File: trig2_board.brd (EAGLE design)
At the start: 80 x 96 mm, 32 parts, among them IC1 SN74ACT244DW, J1 2p-2.54, J10 2p-2.54, J11 2p-2.54, J12 2p-2.54, J13 8pin, J2 2p-2.54, J3 2p-2.54, J4 2p-2.54, J5 2p-2.54, J6 2p-2.54, J7 2p-2.54, J8 2p-2.54, J9 2p-2.54, X1 BU-SMB-V, X10 BU-SMB-V, X11 BU-SMB-V, X12 BU-SMB-V, X13 87758-2816, X14 87758-2816, X15 87758-1616, X16 87758-1616, X17 87758-2816, X18 87758-2816, X2 BU-SMB-V, X3 BU-SMB-V, X4 BU-SMB-V, X5 BU-SMB-V, X6 BU-SMB-V, X7 BU-SMB-V, X8 BU-SMB-V, X9 BU-SMB-V

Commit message: autorouted with topo
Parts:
- removed IC1: SN74ACT244DW, SN74ACT244DW:SOIC127P1030X265-20N
- removed J10, J11, J12, J9: 2p-2.54, Seeed-Connector:H2-2.54
- removed X10, X11, X12, X9: BU-SMB-V, con-coax:BU-SMB-V
- added 106OUT1, 176OUT2, 181OUT3, 183OUT4: BU-SMB-V, con-coax:BU-SMB-V
- added C1: (no value), SparkFun-Capacitors:0805
- added OJ1, OJ2, OJ3, OJ4: 2p-2.54, Seeed-Connector:H2-2.54
- added VSLUE: SN74ACT244DW, SN74ACT244DW:SOIC127P1030X265-20N
- moved J8 40.2 mm to (65.1, 91.0)
- moved X8 40.2 mm to (64.1, 86.0)
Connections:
- removed net IO106: J11.1, X11.1, X14.23
- removed net IO176: J10.1, X10.1, X13.7
- removed net IO181: J9.1, X13.5, X9.1
- removed net IO183: J8.1, X13.3, X8.1
- removed net VCC: IC1.20
- new net IO106_IN1: VSLUE.2, VSLUE.4, X14.23
- new net IO176_IN2: VSLUE.6, VSLUE.8, X13.7
- new net IO181_IN3: VSLUE.11, VSLUE.13, X13.5
- new net IO183_IN4: VSLUE.15, VSLUE.17, X13.3
- new net OUT1: 106OUT1.1, OJ1.1, VSLUE.16, VSLUE.18
- new net OUT2: 176OUT2.1, OJ2.1, VSLUE.12, VSLUE.14
- new net OUT3: 181OUT3.1, OJ3.1, VSLUE.7, VSLUE.9
- new net OUT4: 183OUT4.1, OJ4.1, VSLUE.3, VSLUE.5
- net 5V: now also C1.2, VSLUE.20
- net GND: now also 106OUT1.2, 106OUT1.3, 106OUT1.4, 106OUT1.5, 176OUT2.2, 176OUT2.3, 176OUT2.4, 176OUT2.5, 181OUT3.2, 181OUT3.3, 181OUT3.4, 181OUT3.5, 183OUT4.2, 183OUT4.3, 183OUT4.4, 183OUT4.5, C1.1, OJ1.2, OJ2.2, OJ3.2, OJ4.2, VSLUE.1, VSLUE.10, VSLUE.19; no longer IC1.10, J10.2, J11.2, J12.2, J9.2, X10.2, X10.3, X10.4, X10.5, X11.2, X11.3, X11.4, X11.5, X12.2, X12.3, X12.4, X12.5, X9.2, X9.3, X9.4, X9.5
- net IO102: now also J8.1, X8.1; no longer J12.1, X12.1
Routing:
- net IO106_IN1: track 0.00 -> 82.2 mm
- net IO181_IN3: track 0.00 -> 44.8 mm
- net IO183_IN4: track 0.00 -> 39.7 mm
- net 3V3: track 100.3 -> 64.7 mm, vias 0 -> 2
- net IO106: track 33.4 -> 0.00 mm
- net IO176: track 32.0 -> 0.00 mm
- net 5V: track 128.2 -> 159.8 mm
- net IO176_IN2: track 0.00 -> 30.9 mm
- net IO181: track 23.4 -> 0.00 mm
- net GND: track 0.00 -> 22.1 mm
- net IO183: track 21.0 -> 0.00 mm
- net OUT1: track 0.00 -> 19.2 mm
- net OUT4: track 0.00 -> 17.4 mm
- net OUT2: track 0.00 -> 16.8 mm
- net OUT3: track 0.00 -> 16.7 mm
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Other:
- board size 80 x 96 mm -> 80 x 123 mm
- board text removed: "106"
- board text removed: "176"
- board text removed: "181"
- board text removed: "183"

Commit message: with design block
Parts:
- removed 106OUT1, 176OUT2, 181OUT3, 183OUT4, X7, X8: BU-SMB-V, con-coax:BU-SMB-V
- removed J7, J8: 2p-2.54, Seeed-Connector:H2-2.54
- added 174OUT, 175OUT, 176OUT, 177OUT, 181OUT, 182OUT, 183OUT, 184OUT: BU-SMB-V, con-coax:BU-SMB-V
- added C3: 0.1uF, SparkFun-Capacitors:0805
- added OJ10, OJ11, OJ12, OJ9: 2p-2.54, Seeed-Connector:H2-2.54
- added VSLUE2: SN74ACT244DW, SN74ACT244DW:SOIC127P1030X265-20N
- C1: value (none) -> 0.1uF
- moved OJ1 105.6 mm to (120.0, 72.9), turned to 0 degrees
- moved OJ2 101.8 mm to (120.0, 63.0), turned to 0 degrees
- moved C1 91.4 mm to (107.0, 78.0), turned to 270 degrees
- moved VSLUE 79.7 mm to (102.0, 69.0), turned to 0 degrees
- moved J6 67.3 mm to (5.79, 7.95), turned to 0 degrees
- moved X6 63.5 mm to (10.7, 6.91), turned to 90 degrees
- moved OJ4 60.0 mm to (84.0, 73.1), turned to 0 degrees
- moved J5 58.7 mm to (5.79, 18.0), turned to 0 degrees
- moved J13 56.5 mm to (56.0, 77.0), turned to 0 degrees
- moved J1 56.1 mm to (5.79, 58.2), turned to 0 degrees
- moved X14 54.9 mm to (73.0, 18.0), turned to 270 degrees
- moved X5 53.9 mm to (10.7, 17.0), turned to 90 degrees
- moved OJ3 53.0 mm to (84.0, 63.0), turned to 0 degrees
- moved J4 52.6 mm to (5.79, 28.1), turned to 0 degrees
- moved J2 51.1 mm to (5.79, 48.2), turned to 0 degrees
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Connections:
- removed net IO100: J7.1, X14.27, X7.1
- removed net IO102: J8.1, X14.25, X8.1
- removed net IO106_IN1: VSLUE.2, VSLUE.4, X14.23
- new net IO174_IN1: VSLUE.2, VSLUE.4, X13.9
- new net IO175_IN1: VSLUE2.2, VSLUE2.4, X13.10
- new net IO177_IN2: VSLUE2.6, VSLUE2.8, X13.8
- new net IO182_IN3: VSLUE2.11, VSLUE2.13, X13.6
- new net IO184_IN4: VSLUE2.15, VSLUE2.17, X13.4
- new net OUT5: 175OUT.1, OJ12.1, VSLUE2.16, VSLUE2.18
- new net OUT6: 177OUT.1, OJ11.1, VSLUE2.12, VSLUE2.14
- new net OUT7: 182OUT.1, OJ10.1, VSLUE2.7, VSLUE2.9
- new net OUT8: 184OUT.1, OJ9.1, VSLUE2.3, VSLUE2.5
- net 3V3: no longer X18.2
- net 5V: now also C3.2, J13.7, VSLUE2.20; no longer J13.1
- net GND: now also 174OUT.2, 174OUT.3, 174OUT.4, 174OUT.5, 175OUT.2, 175OUT.3, 175OUT.4, 175OUT.5, 176OUT.2, 176OUT.3, 176OUT.4, 176OUT.5, 177OUT.2, 177OUT.3, 177OUT.4, 177OUT.5, 181OUT.2, 181OUT.3, 181OUT.4, 181OUT.5, 182OUT.2, 182OUT.3, 182OUT.4, 182OUT.5, 183OUT.2, 183OUT.3, 183OUT.4, 183OUT.5, 184OUT.2, 184OUT.3, 184OUT.4, 184OUT.5, C3.1, J13.5, J13.6, OJ10.2, OJ11.2, OJ12.2, OJ9.2, VSLUE2.1, VSLUE2.10, VSLUE2.19; no longer 106OUT1.2, 106OUT1.3, 106OUT1.4, 106OUT1.5, 176OUT2.2, 176OUT2.3, 176OUT2.4, 176OUT2.5, 181OUT3.2, 181OUT3.3, 181OUT3.4, 181OUT3.5, 183OUT4.2, 183OUT4.3, 183OUT4.4, 183OUT4.5, J13.2, J13.7, J7.2, J8.2, X7.2, X7.3, X7.4, X7.5, X8.2, X8.3, X8.4, X8.5
- net IO186: now also J13.1; no longer J13.3
- net IO188: now also J13.2; no longer J13.4
- net IO194: now also J13.3; no longer J13.5
- net IO196: now also J13.4; no longer J13.6
- net OUT1: now also 174OUT.1; no longer 106OUT1.1
- net OUT2: now also 176OUT.1; no longer 176OUT2.1
- net OUT3: now also 181OUT.1; no longer 181OUT3.1
- net OUT4: now also 183OUT.1; no longer 183OUT4.1
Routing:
- net IO106_IN1: track 82.2 -> 0.00 mm
- net IO182_IN3: track 0.00 -> 57.5 mm
- net IO174_IN1: track 0.00 -> 47.1 mm
- net 3V3: track 64.7 -> 21.2 mm, vias 2 -> 0
- net IO184_IN4: track 0.00 -> 41.2 mm, vias 0 -> 1
- net IO175_IN1: track 0.00 -> 39.2 mm
- net IO177_IN2: track 0.00 -> 32.4 mm
- net GND: track 22.1 -> 49.0 mm
- net IO102: track 24.3 -> 0.00 mm
- net OUT8: track 0.00 -> 23.8 mm
- net OUT5: track 0.00 -> 23.8 mm
- net OUT6: track 0.00 -> 23.3 mm
- net OUT7: track 0.00 -> 23.2 mm
- net IO100: track 21.1 -> 0.00 mm
- net IO183_IN4: track 39.7 -> 57.6 mm, vias 0 -> 1
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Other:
- board size 80 x 123 mm -> 123 x 80 mm
- board text removed: "100"
- board text removed: "102"

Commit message: better routing
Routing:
- net IO183_IN4: track 57.6 -> 42.7 mm
- net OUT4: track 28.8 -> 18.7 mm
- net IO182_IN3: track 57.5 -> 48.4 mm, vias 0 -> 1
- net OUT7: track 23.2 -> 18.0 mm
- net OUT8: track 23.8 -> 18.7 mm
- net IO176_IN2: track 41.6 -> 36.5 mm
- net GND: track 49.0 -> 53.3 mm
- net IO175_IN1: track 39.2 -> 35.0 mm
- net IO181_IN3: track 45.9 -> 41.7 mm
- net OUT6: track 23.3 -> 19.2 mm
- net OUT5: track 23.8 -> 20.0 mm
- net IO177_IN2: track 32.4 -> 29.3 mm
- net IO194: track 24.5 -> 21.5 mm
- net 3V3: track 21.2 -> 18.8 mm
- net OUT1: track 19.1 -> 21.5 mm, vias 0 -> 1
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
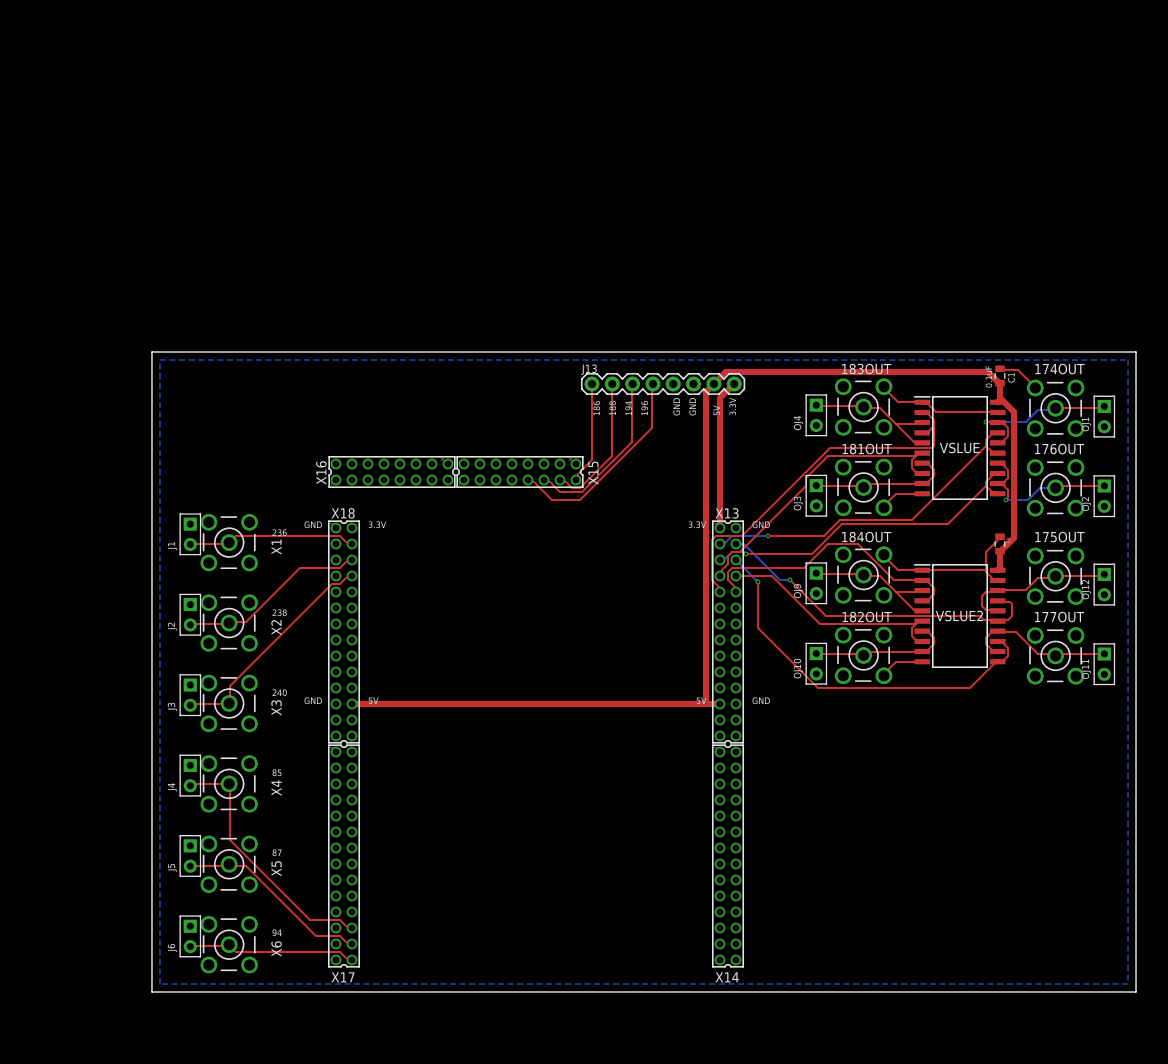
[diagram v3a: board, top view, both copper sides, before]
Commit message: 16 inputs and 16 outputs
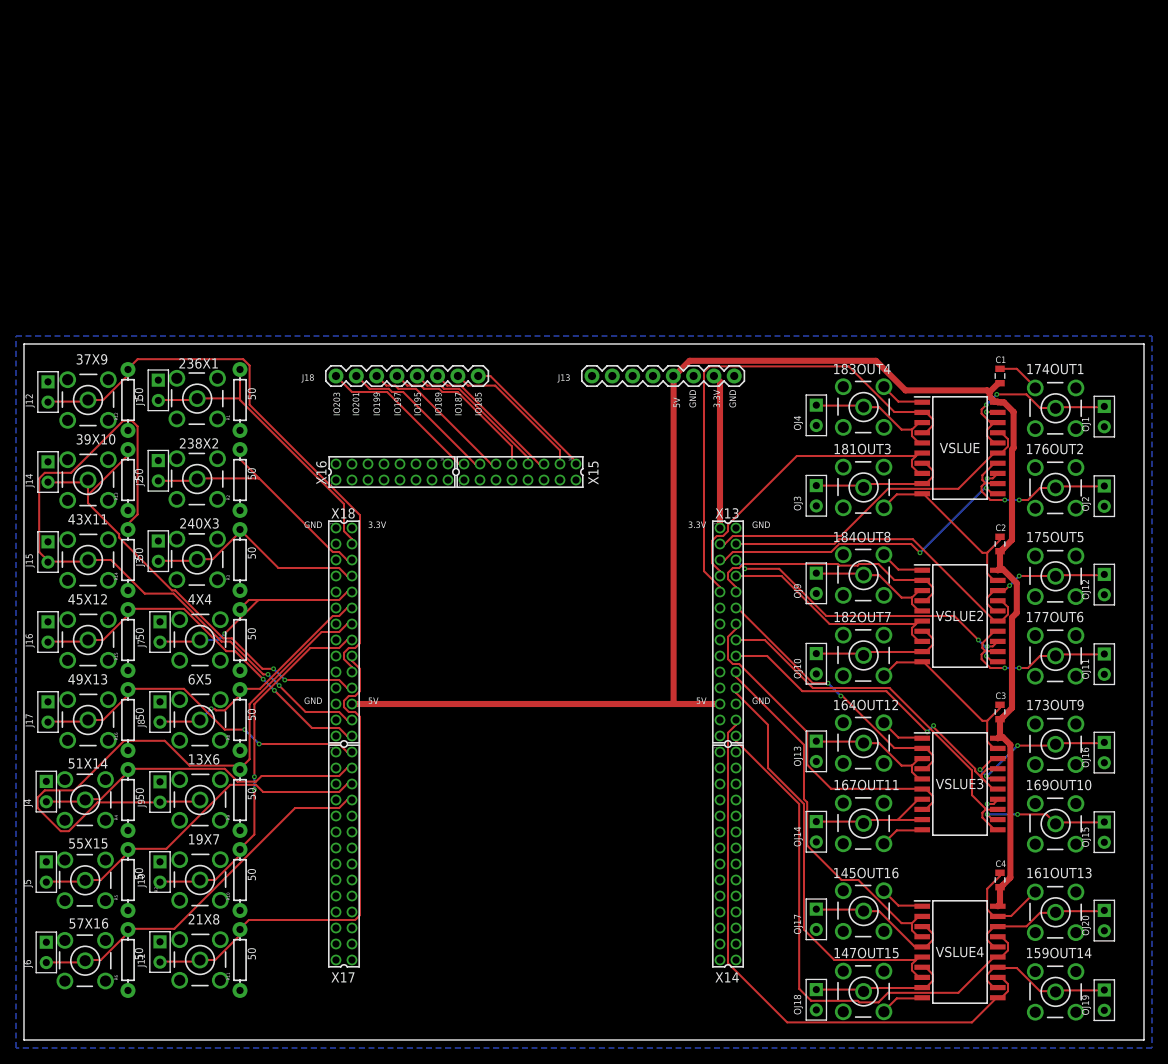
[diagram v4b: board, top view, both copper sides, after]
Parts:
- removed X1, X2, X3, X4, X5, X6: BU-SMB-V, con-coax:BU-SMB-V
- added 13X6, 145OUT16, 147OUT15, 159OUT14, 161OUT13, 164OUT12, 167OUT11, 169OUT10, 173OUT9, 19X7, 21X8, 236X1, 238X2, 240X3, 37X9, 39X10, 43X11, 45X12, 49X13, 4X4, 51X14, 55X15, 57X16, 6X5: BU-SMB-V, con-coax:BU-SMB-V
- added C2, C4: 0.1uF, SparkFun-Capacitors:0805
- added J10, J11, J12, J14, J15, J16, J17, J7, J8, J9, OJ13, OJ14, OJ15, OJ16, OJ17, OJ18, OJ19, OJ20: 2p-2.54, Seeed-Connector:H2-2.54
- added J18: 8pin, SparkFun-Connectors:1X08
- added R1, R10, R11, R12, R13, R14, R15, R16, R2, R3, R4, R5, R6, R7, R8, R9: 50, SparkFun-Passives:AXIAL-0.3
- added VSLUE3, VSLUE4: SN74ACT244DW, SN74ACT244DW:SOIC127P1030X265-20N
- moved C3 21.0 mm to (107.0, 36.0)
- moved J2 18.4 mm to (1.79, 66.2)
- moved J3 18.4 mm to (1.79, 56.1)
- moved J1 18.4 mm to (1.79, 76.2)
- moved J4 18.1 mm to (-12.2, 26.1)
- moved J5 18.1 mm to (-12.2, 16.0)
- moved J6 18.1 mm to (-12.2, 5.95)
- moved J13 1.00 mm to (56.0, 78.0)
- renumbered 174OUT to 174OUT1, 175OUT to 175OUT5, 176OUT to 176OUT2, 177OUT to 177OUT6, 181OUT to 181OUT3, 182OUT to 182OUT7, 183OUT to 183OUT4, 184OUT to 184OUT8
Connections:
- removed net IO186: J13.1, X15.15
- removed net IO188: J13.2, X15.13
- removed net IO194: J13.3, X15.11
- removed net IO196: J13.4, X15.9
- removed net IO85: J4.2, X17.24, X4.1
- removed net IO87: J5.2, X17.26, X5.1
- removed net IO94: J6.2, X17.28, X6.1
- new net IO13: 13X6.1, J9.2, R9.P$2, X18.14
- new net IO145_IN4: VSLUE4.15, VSLUE4.17, X13.28
- new net IO147_IN3: VSLUE4.11, VSLUE4.13, X13.26
- new net IO159_IN2: VSLUE4.6, VSLUE4.8, X13.22
- new net IO161_IN1: VSLUE4.2, VSLUE4.4, X13.20
- new net IO164_IN4: VSLUE3.15, VSLUE3.17, X13.18
- new net IO167_IN3: VSLUE3.11, VSLUE3.13, X13.16
- new net IO169_IN2: VSLUE3.6, VSLUE3.8, X13.14
- new net IO173_IN1: VSLUE3.2, VSLUE3.4, X13.12
- new net IO185: J18.8, X15.16
- new net IO187: J18.7, X15.14
- new net IO189: J18.6, X15.12
- new net IO19: 19X7.1, J10.2, R10.P$2, X18.16
- new net IO195: J18.5, X15.10
- new net IO197: J18.4, X15.8
- new net IO199: J18.3, X15.6
- new net IO201: J18.2, X15.4
- new net IO203: J18.1, X15.2
- new net IO21: 21X8.1, J11.2, R11.P$2, X18.18
- new net IO37: 37X9.1, J12.2, R12.P$2, X18.20
- new net IO39: 39X10.1, J14.2, R13.P$2, X18.22
- new net IO4: 4X4.1, J7.2, R7.P$2, X18.10
- new net IO43: 43X11.1, J15.2, R14.P$2, X18.26
- new net IO45: 45X12.1, J16.2, R15.P$2, X18.28
- new net IO49: 49X13.1, J17.2, R16.P$2, X17.2
- new net IO51: 51X14.1, J4.2, R4.P$2, X17.4
- new net IO55: 55X15.1, J5.2, R5.P$2, X17.6
- new net IO57: 57X16.1, J6.2, R6.P$2, X17.8
- new net IO6: 6X5.1, J8.2, R8.P$2, X18.12
- new net OUT10: 169OUT10.1, OJ15.1, VSLUE3.12, VSLUE3.14
- new net OUT11: 167OUT11.1, OJ14.1, VSLUE3.7, VSLUE3.9
- new net OUT12: 164OUT12.1, OJ13.1, VSLUE3.3, VSLUE3.5
- new net OUT13: 161OUT13.1, OJ20.1, VSLUE4.16, VSLUE4.18
- new net OUT14: 159OUT14.1, OJ19.1, VSLUE4.12, VSLUE4.14
- new net OUT15: 147OUT15.1, OJ18.1, VSLUE4.7, VSLUE4.9
- new net OUT16: 145OUT16.1, OJ17.1, VSLUE4.3, VSLUE4.5
- new net OUT9: 173OUT9.1, OJ16.1, VSLUE3.16, VSLUE3.18
- net 3V3: now also J13.7; no longer J13.8
- net 5V: now also C2.2, C4.2, J13.5, VSLUE3.20, VSLUE4.20; no longer J13.7
- net GND: now also 13X6.2, 13X6.3, 13X6.4, 13X6.5, 145OUT16.2, 145OUT16.3, 145OUT16.4, 145OUT16.5, 147OUT15.2, 147OUT15.3, 147OUT15.4, 147OUT15.5, 159OUT14.2, 159OUT14.3, 159OUT14.4, 159OUT14.5, 161OUT13.2, 161OUT13.3, 161OUT13.4, 161OUT13.5, 164OUT12.2, 164OUT12.3, 164OUT12.4, 164OUT12.5, 167OUT11.2, 167OUT11.3, 167OUT11.4, 167OUT11.5, 169OUT10.2, 169OUT10.3, 169OUT10.4, 169OUT10.5, 173OUT9.2, 173OUT9.3, 173OUT9.4, 173OUT9.5, 19X7.2, 19X7.3, 19X7.4, 19X7.5, 21X8.2, 21X8.3, 21X8.4, 21X8.5, 236X1.2, 236X1.3, 236X1.4, 236X1.5, 238X2.2, 238X2.3, 238X2.4, 238X2.5, 240X3.2, 240X3.3, 240X3.4, 240X3.5, 37X9.2, 37X9.3, 37X9.4, 37X9.5, 39X10.2, 39X10.3, 39X10.4, 39X10.5, 43X11.2, 43X11.3, 43X11.4, 43X11.5, 45X12.2, 45X12.3, 45X12.4, 45X12.5, 49X13.2, 49X13.3, 49X13.4, 49X13.5, 4X4.2, 4X4.3, 4X4.4, 4X4.5, 51X14.2, 51X14.3, 51X14.4, 51X14.5, 55X15.2, 55X15.3, 55X15.4, 55X15.5, 57X16.2, 57X16.3, 57X16.4, 57X16.5, 6X5.2, 6X5.3, 6X5.4, 6X5.5, C2.1, C4.1, J10.1, J11.1, J12.1, J13.8, J14.1, J15.1, J16.1, J17.1, J7.1, J8.1, J9.1, OJ13.2, OJ14.2, OJ15.2, OJ16.2, OJ17.2, OJ18.2, OJ19.2, OJ20.2, R1.P$1, R10.P$1, R11.P$1, R12.P$1, R13.P$1, R14.P$1, R15.P$1, R16.P$1, R2.P$1, R3.P$1, R4.P$1, R5.P$1, R6.P$1, R7.P$1, R8.P$1, R9.P$1, VSLUE3.1, VSLUE3.10, VSLUE3.19, VSLUE4.1, VSLUE4.10, VSLUE4.19; no longer J13.5, X1.2, X1.3, X1.4, X1.5, X2.2, X2.3, X2.4, X2.5, X3.2, X3.3, X3.4, X3.5, X4.2, X4.3, X4.4, X4.5, X5.2, X5.3, X5.4, X5.5, X6.2, X6.3, X6.4, X6.5
- net IO236: now also 236X1.1, R1.P$2; no longer X1.1
- net IO238: now also 238X2.1, R2.P$2; no longer X2.1
- net IO240: now also 240X3.1, R3.P$2; no longer X3.1
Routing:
- net IO43: track 0.00 -> 86.3 mm, vias 0 -> 2
- net IO13: track 0.00 -> 80.5 mm
- net IO37: track 0.00 -> 74.0 mm
- net IO147_IN3: track 0.00 -> 73.0 mm
- net IO145_IN4: track 0.00 -> 66.9 mm
- net IO21: track 0.00 -> 63.3 mm
- net IO39: track 0.00 -> 58.7 mm, vias 0 -> 2
- net IO159_IN2: track 0.00 -> 53.3 mm
- net 5V: track 149.2 -> 202.2 mm
- net IO45: track 0.00 -> 47.8 mm, vias 0 -> 2
- net GND: track 53.3 -> 100.8 mm, vias 0 -> 1
- net IO57: track 0.00 -> 47.5 mm
- net IO167_IN3: track 0.00 -> 47.1 mm
- net IO161_IN1: track 0.00 -> 46.6 mm
- net IO19: track 0.00 -> 46.6 mm, vias 0 -> 2
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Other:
- board size 123 x 80 mm -> 140 x 87 mm
- board text added: "IO185"
- board text added: "IO187"
- board text added: "IO189"
- board text added: "IO195"
- board text added: "IO197"
- board text added: "IO199"
- board text added: "IO201"
- board text added: "IO203"
- board text removed: "186"
- board text removed: "188"
- board text removed: "194"
- board text removed: "196"
- board text removed: "236"
- board text removed: "238"
- board text removed: "240"
- board text removed: "85"
- board text removed: "87"
- board text removed: "94"
